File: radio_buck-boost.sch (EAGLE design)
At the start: 21 parts, among them IC1 TPS6300, J1 FTDI_DEVICE, U1 ATMEGA328P_TQFP, U2 GY-521MPU6050

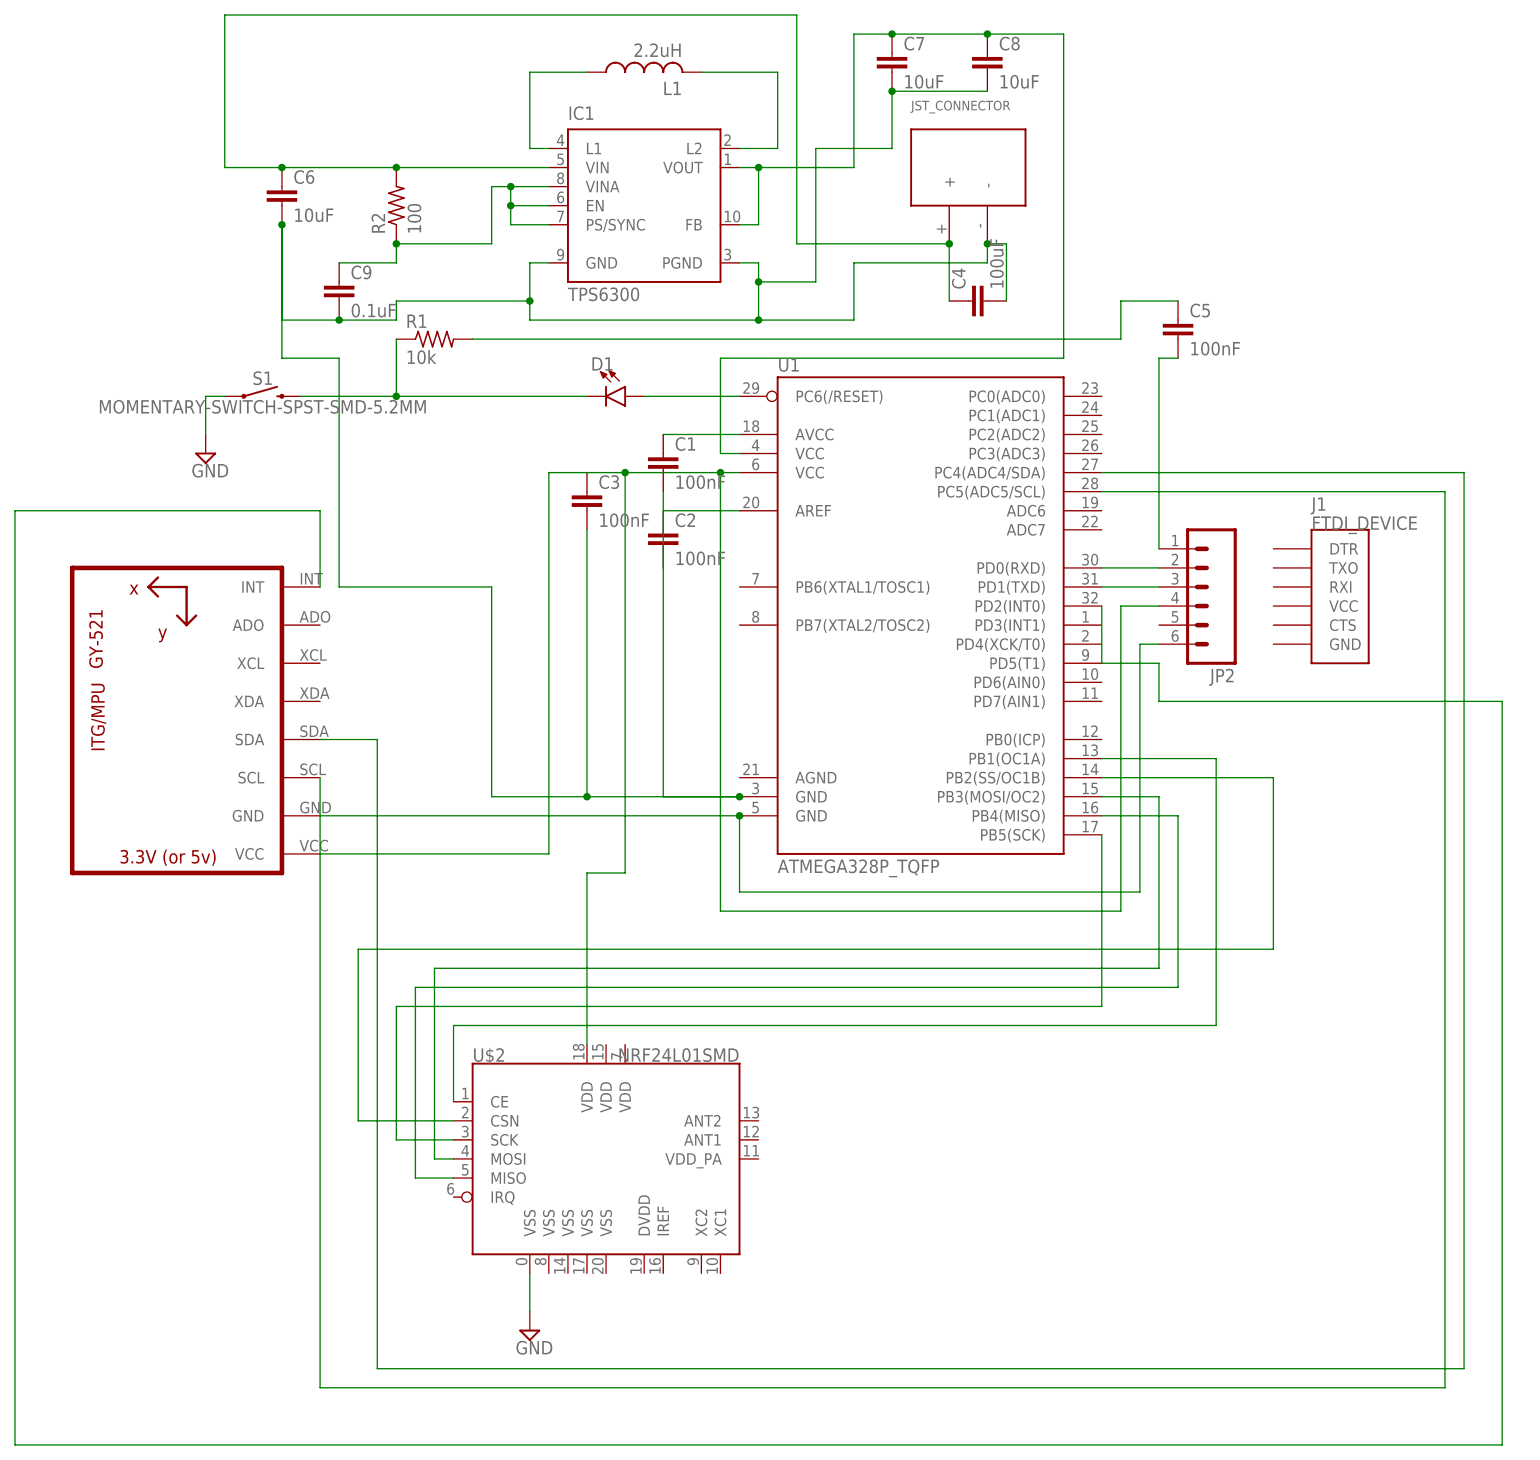
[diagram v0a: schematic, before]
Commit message: Added separate radio & buck boost sch
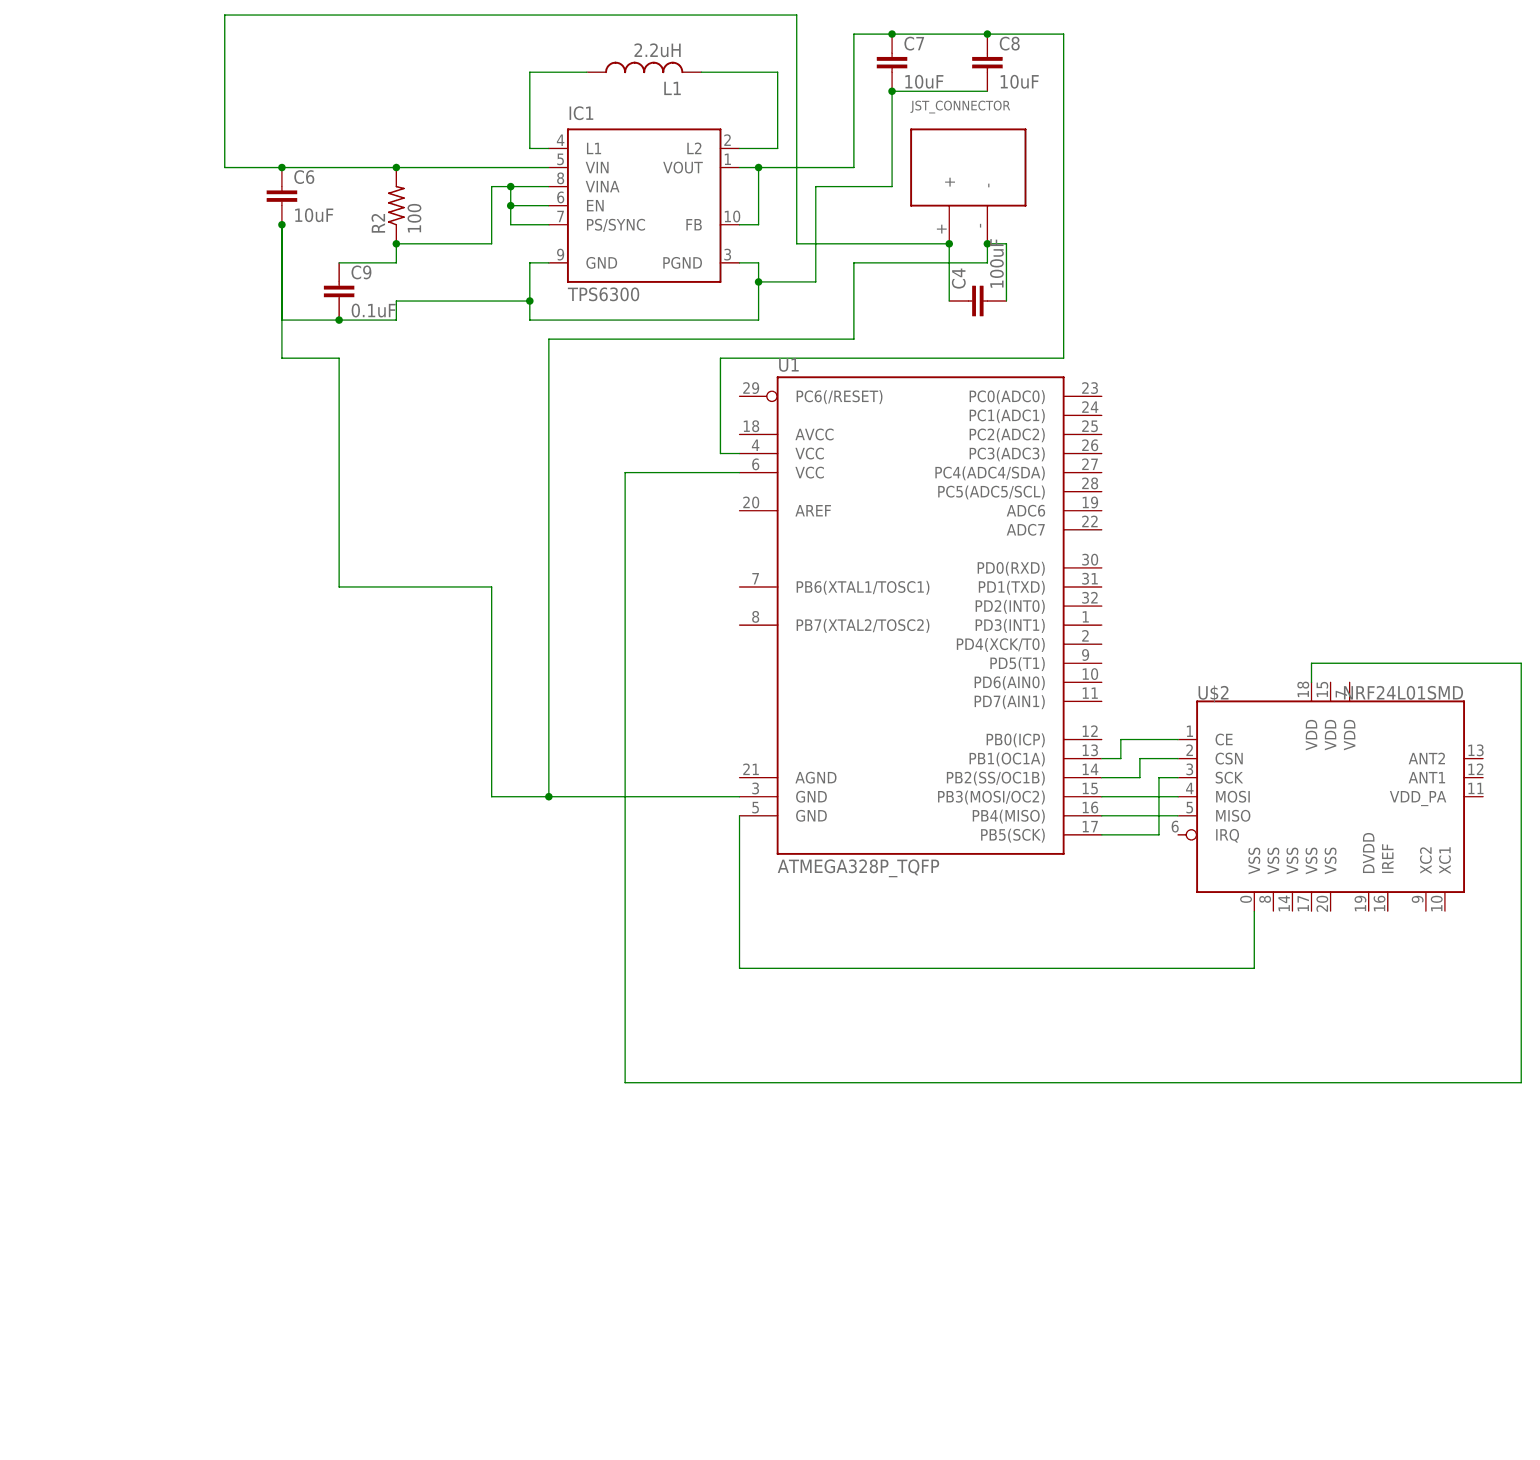
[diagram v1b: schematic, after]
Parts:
- removed C1, C2, C3, C5: 100nF, rcl:C-EUC0603
- removed D1: (no value), SparkFun-LED:LED0603
- removed J1: FTDI_DEVICE, quad:FTDI_DEVICE
- removed JP2: (no value), SparkFun:M06SMD-FEMALE-V2
- removed R1: 10k, resistor:R-US_R0603
- removed S1: MOMENTARY-SWITCH-SPST-SMD-5.2MM, SparkFun-Switches:MOMENTARY-SWITCH-SPST-SMD-5.2MM
- removed U2: GY-521MPU6050, quad:GY-521MPU6050
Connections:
- removed net GND: S1.1, U$2.VSS@0
- removed net N$11: C5.1, R1.2
- removed net N$12: D1.A, U1.PC6(/RESET)
- removed net N$13: D1.C, R1.1, S1.2
- removed net N$16: C3.1, JP2.4, U$2.VDD@18, U1.VCC@6, U2.VCC
- removed net N$17: U1.PC5(ADC5/SCL), U2.SCL
- removed net N$18: U1.PC4(ADC4/SDA), U2.SDA
- removed net N$19: U1.PD2(INT0), U2.INT
- removed net N$3 (its old number): JP2.2, U1.PD0(RXD)
- removed net N$4 (its old number): JP2.3, U1.PD1(TXD)
- removed net N$7: C1.2, C2.2, C3.2, C4.2, C6.2, C7.2, C8.2, C9.2, IC1G$1.GND, IC1G$1.PGND, U$1.-, U1.GND@3
- removed net N$9 (its old number): JP2.6, U1.GND@5, U2.GND
- net N$1: now also U$2.VDD@18, U1.VCC@6; no longer C1.1, U1.AVCC
- net N$10: now also C4.2, C6.2, C7.2, C8.2, C9.2, IC1G$1.GND, IC1G$1.PGND, U$1.-, U1.GND@3; no longer C5.2, JP2.1
- net N$2: now also U$2.VSS@0, U1.GND@5; no longer C2.1, U1.AREF
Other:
- moved on the sheet: U$2

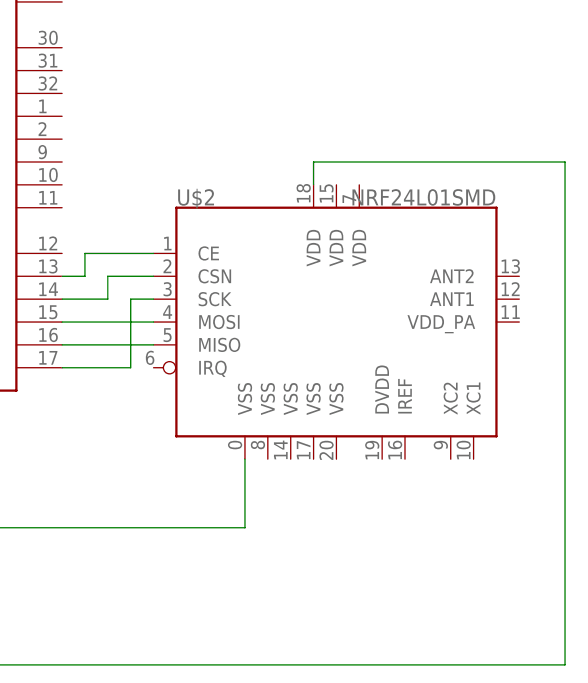
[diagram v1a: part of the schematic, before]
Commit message: Added decoupling capacitors to radio module
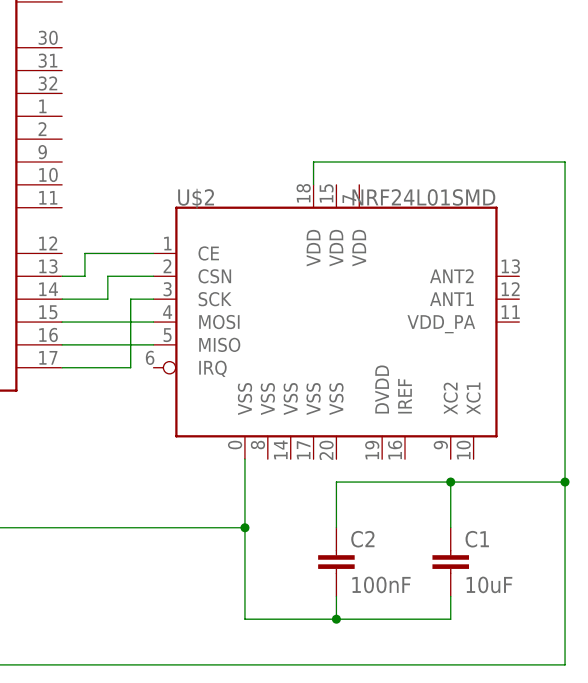
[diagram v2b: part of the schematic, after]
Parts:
- added C1: 10uF, rcl:C-EUC0603
- added C2: 100nF, rcl:C-EUC0603
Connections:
- removed net N$2: U$2.VSS@0, U1.GND@5
- new net N$11: C1.2, C2.2, U$2.VSS@0, U1.GND@5
- net N$1: now also C1.1, C2.1
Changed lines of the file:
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@@
 <part name="C9" library="rcl" library_urn="urn:adsk.eagle:library:334" deviceset="C-EU" device="C0603" package3d_urn="urn:adsk.eagle:package:23616/2" value="0.1uF"/>
 <part name="U$1" library="quad" deviceset="JST_CONNECTOR_FEMALE" device=""/>
+<part name="C1" library="rcl" library_urn="urn:adsk.eagle:library:334" deviceset="C-EU" device="C0603" package3d_urn="urn:adsk.eagle:package:23616/2" value="10uF"/>
+<part name="C2" library="rcl" library_urn="urn:adsk.eagle:library:334" deviceset="C-EU" device="C0603" package3d_urn="urn:adsk.eagle:package:23616/2" value="100nF"/>
 </parts>
 <sheets>
@@
 <instance part="C9" gate="G$1" x="-15.24" y="83.82"/>
 <instance part="U$1" gate="G$1" x="68.58" y="99.06"/>
+<instance part="C1" gate="G$1" x="129.54" y="-10.16"/>
+<instance part="C2" gate="G$1" x="116.84" y="-10.16"/>
 </instances>
 <busses>
@@
 <wire x1="114.3" y1="30.48" x2="114.3" y2="33.02" width="0.1524" layer="91"/>
 <wire x1="114.3" y1="33.02" x2="142.24" y2="33.02" width="0.1524" layer="91"/>
-<wire x1="142.24" y1="33.02" x2="142.24" y2="-22.86" width="0.1524" layer="91"/>
+<wire x1="142.24" y1="33.02" x2="142.24" y2="-2.54" width="0.1524" layer="91"/>
 <pinref part="U1" gate="U$1" pin="VCC@6"/>
+<wire x1="142.24" y1="-2.54" x2="142.24" y2="-22.86" width="0.1524" layer="91"/>
 <wire x1="22.86" y1="58.42" x2="38.1" y2="58.42" width="0.1524" layer="91"/>
 <wire x1="22.86" y1="-22.86" x2="22.86" y2="58.42" width="0.1524" layer="91"/>
 <wire x1="142.24" y1="-22.86" x2="22.86" y2="-22.86" width="0.1524" layer="91"/>
-</segment>
-</net>
-<net name="N$2" class="0">
-<segment>
-<pinref part="U$2" gate="G$1" pin="VSS@0"/>
-<wire x1="106.68" y1="0" x2="106.68" y2="-7.62" width="0.1524" layer="91"/>
-<pinref part="U1" gate="U$1" pin="GND@5"/>
-<wire x1="106.68" y1="-7.62" x2="38.1" y2="-7.62" width="0.1524" layer="91"/>
-<wire x1="38.1" y1="-7.62" x2="38.1" y2="12.7" width="0.1524" layer="91"/>
+<pinref part="C1" gate="G$1" pin="1"/>
+<wire x1="142.24" y1="-2.54" x2="129.54" y2="-2.54" width="0.1524" layer="91"/>
+<wire x1="129.54" y1="-2.54" x2="129.54" y2="-7.62" width="0.1524" layer="91"/>
+<junction x="142.24" y="-2.54"/>
+<pinref part="C2" gate="G$1" pin="1"/>
+<wire x1="129.54" y1="-2.54" x2="116.84" y2="-2.54" width="0.1524" layer="91"/>
+<wire x1="116.84" y1="-2.54" x2="116.84" y2="-7.62" width="0.1524" layer="91"/>
+<junction x="129.54" y="-2.54"/>
 </segment>
 </net>
@@
 </segment>
 </net>
+<net name="N$11" class="0">
+<segment>
+<pinref part="C1" gate="G$1" pin="2"/>
+<wire x1="129.54" y1="-15.24" x2="129.54" y2="-17.78" width="0.1524" layer="91"/>
+<pinref part="U$2" gate="G$1" pin="VSS@0"/>
+<wire x1="106.68" y1="0" x2="106.68" y2="-7.62" width="0.1524" layer="91"/>
+<pinref part="U1" gate="U$1" pin="GND@5"/>
+<wire x1="106.68" y1="-7.62" x2="38.1" y2="-7.62" width="0.1524" layer="91"/>
+<wire x1="38.1" y1="-7.62" x2="38.1" y2="12.7" width="0.1524" layer="91"/>
+<pinref part="C2" gate="G$1" pin="2"/>
+<wire x1="116.84" y1="-15.24" x2="116.84" y2="-17.78" width="0.1524" layer="91"/>
+<wire x1="116.84" y1="-17.78" x2="106.68" y2="-17.78" width="0.1524" layer="91"/>
+<wire x1="106.68" y1="-17.78" x2="106.68" y2="-7.62" width="0.1524" layer="91"/>
+<junction x="106.68" y="-7.62"/>
+<wire x1="129.54" y1="-17.78" x2="116.84" y2="-17.78" width="0.1524" layer="91"/>
+<junction x="116.84" y="-17.78"/>
+</segment>
+</net>
